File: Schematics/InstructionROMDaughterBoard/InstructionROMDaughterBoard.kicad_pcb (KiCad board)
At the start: 4 copper layers, 62.2 x 49.5 mm, 9 parts, among them J1 PC/IF Connector [0..7], J2 PC/IF Connector [8..15], J3 IROM Connector [0..7], J4 IROM Connector [8..15], U1 GLS29EE010, U2 GLS29EE010

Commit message: Instruction ROM daughter board uses same basic PCB design settings as the main board.
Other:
- net class Default: clearance 0.2 -> 0.127; trace_width 0.25 -> 0.127; via_dia 0.8 -> 0.45; via_drill 0.4 -> 0.3
- rule trace_clearance: 0.2 -> 0.127
- rule trace_min: 0.2 -> 0.0889
- rule via_min_drill: 0.3 -> 0.2
- rule via_min_size: 0.4 -> 0.45
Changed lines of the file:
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@@
   )
   (setup
-    (last_trace_width 0.25)
-    (trace_clearance 0.2)
+    (last_trace_width 0.127)
+    (trace_clearance 0.127)
     (zone_clearance 0.508)
     (zone_45_only no)
-    (trace_min 0.2)
-    (via_size 0.8)
-    (via_drill 0.4)
-    (via_min_size 0.4)
-    (via_min_drill 0.3)
+    (trace_min 0.0889)
+    (via_size 0.45)
+    (via_drill 0.3)
+    (via_min_size 0.45)
+    (via_min_drill 0.2)
     (uvia_size 0.3)
     (uvia_drill 0.1)
@@
   (net 34 /IROM8)
   (net_class Default "This is the default net class."
-    (clearance 0.2)
-    (trace_width 0.25)
-    (via_dia 0.8)
-    (via_drill 0.4)
+    (clearance 0.127)
+    (trace_width 0.127)
+    (via_dia 0.45)
+    (via_drill 0.3)
     (uvia_dia 0.3)
     (uvia_drill 0.1)
@@
     (add_net /PC_IF9)
     (add_net GND)
-    (add_net "Net-(U1-Pad1)")
-    (add_net "Net-(U1-Pad30)")
-    (add_net "Net-(U2-Pad1)")
-    (add_net "Net-(U2-Pad30)")
     (add_net VCC)
   )

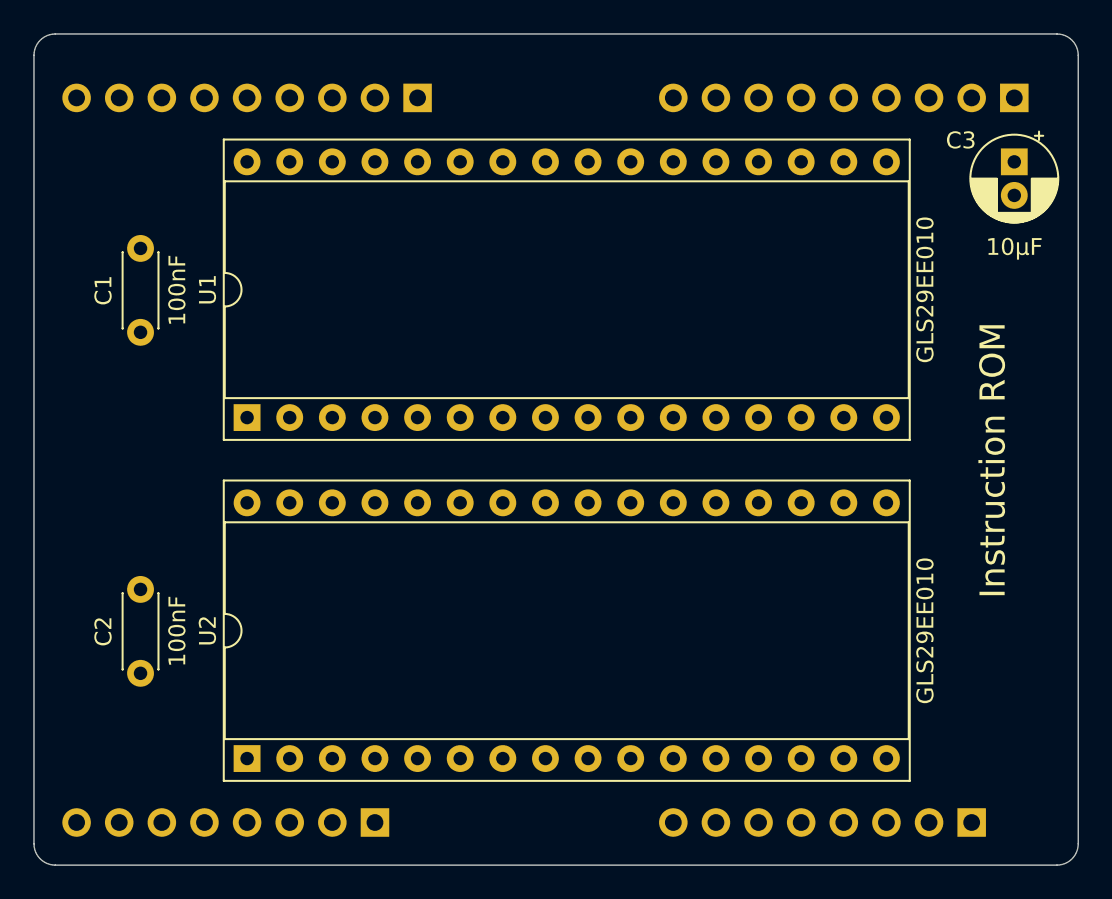
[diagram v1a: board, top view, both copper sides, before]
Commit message: checkpoint: laying out instruction rom daughter board and added power planes.
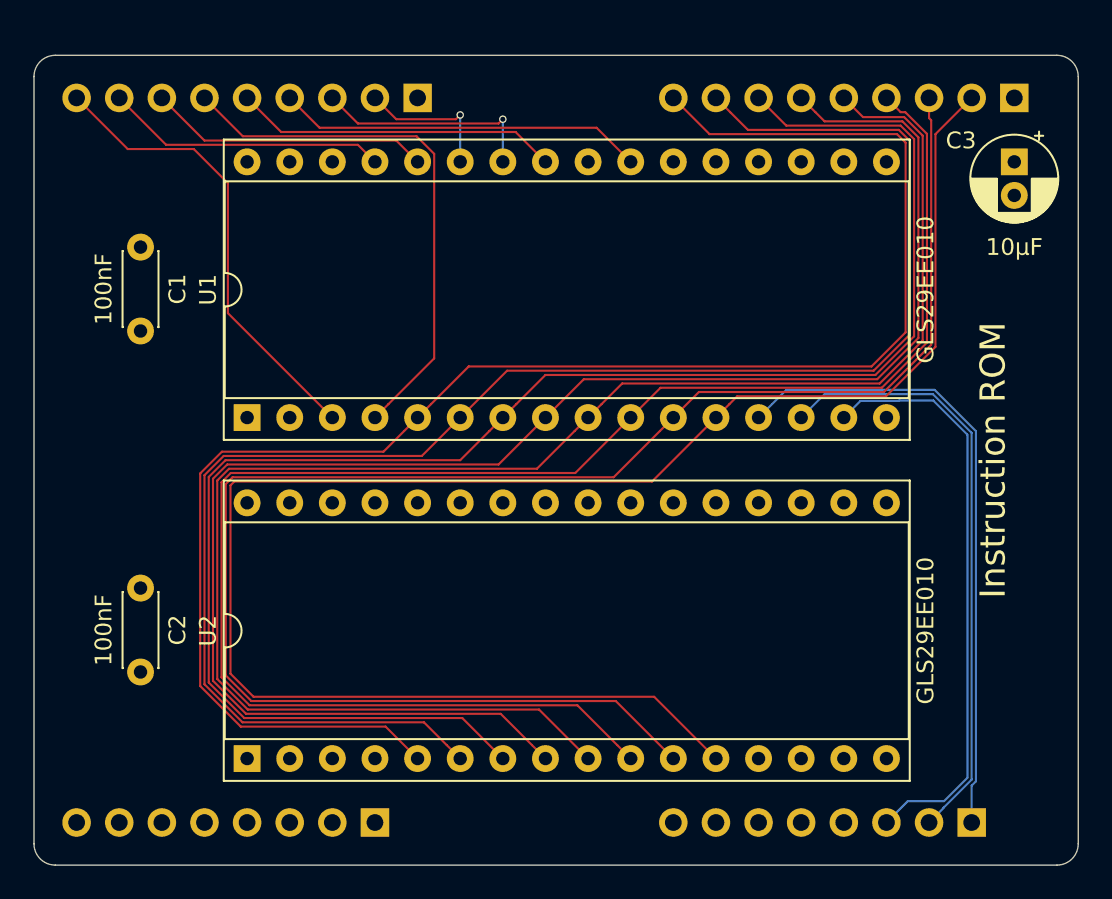
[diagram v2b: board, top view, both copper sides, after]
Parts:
- moved C1 5.08 mm to (118.1, 64.8), turned to 270 degrees
- moved C2 5.08 mm to (118.1, 85.1), turned to 270 degrees
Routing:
- net /PC_IF0: track 0.00 -> 103.4 mm
- net /PC_IF1: track 0.00 -> 100.4 mm
- net /PC_IF2: track 0.00 -> 99.2 mm
- net /PC_IF3: track 0.00 -> 99.2 mm
- net /PC_IF5: track 0.00 -> 99.2 mm
- net /PC_IF4: track 0.00 -> 99.2 mm
- net /PC_IF6: track 0.00 -> 99.2 mm
- net /PC_IF7: track 0.00 -> 99.2 mm
- net /IROM0: track 0.00 -> 38.1 mm
- net /IROM1: track 0.00 -> 36.0 mm
- net /IROM2: track 0.00 -> 35.0 mm
- net /PC_IF12: track 0.00 -> 32.2 mm
- net /PC_IF15: track 0.00 -> 27.7 mm
- net /PC_IF10: track 0.00 -> 21.9 mm
- net /PC_IF11: track 0.00 -> 19.4 mm
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- added copper zone on GND.Cu, net GND
- added copper zone on VCC.Cu, net VCC
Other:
- board size 62.2 x 49.5 mm -> 62.2 x 48.3 mm

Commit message: Finish routing Instruction ROM daughter board PCB.
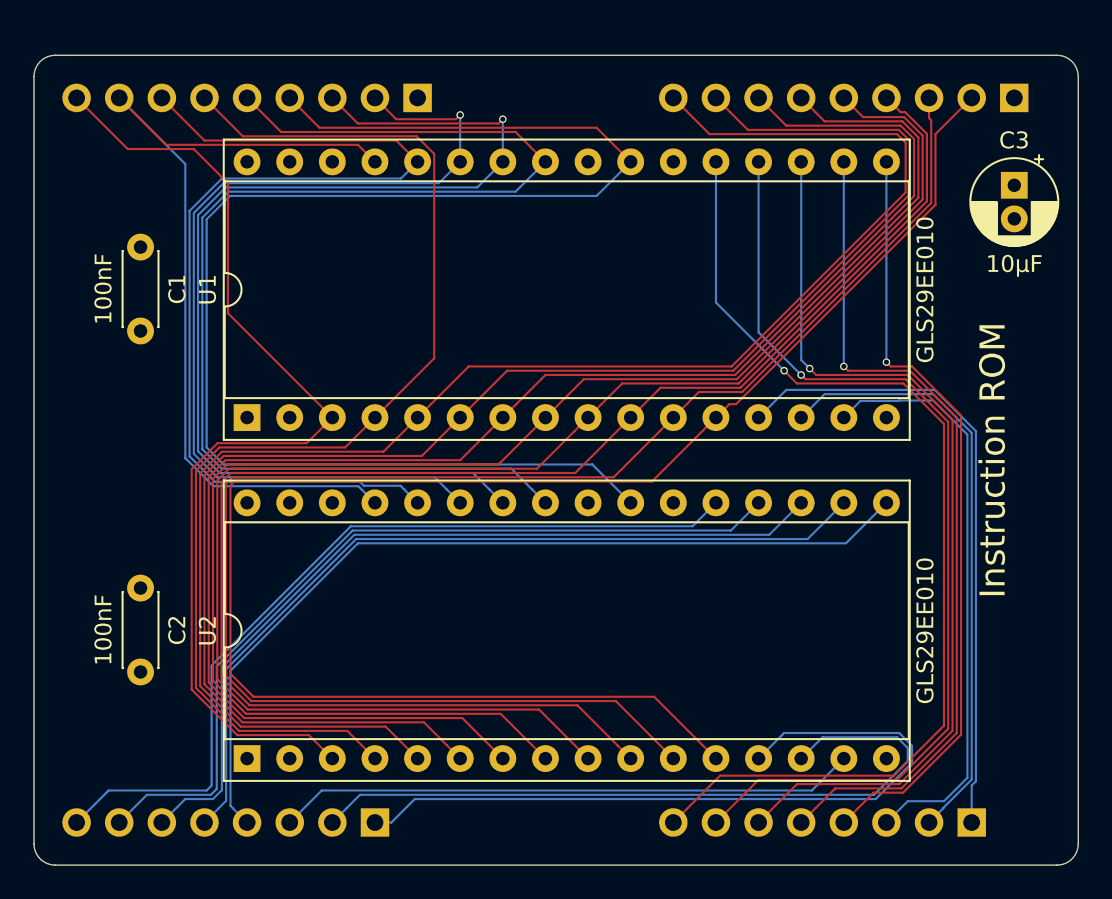
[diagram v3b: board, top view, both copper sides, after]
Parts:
- moved C3 1.40 mm to (170.2, 61.1)
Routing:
- net /PC_IF10: track 21.9 -> 88.8 mm
- net /IROM7: track 0.00 -> 61.5 mm, vias 0 -> 1
- net /IROM6: track 0.00 -> 58.1 mm, vias 0 -> 1
- net /PC_IF11: track 19.4 -> 76.8 mm
- net /IROM5: track 0.00 -> 54.7 mm, vias 0 -> 1
- net /PC_IF9: track 13.4 -> 66.4 mm
- net /IROM11: track 0.00 -> 52.7 mm
- net /IROM12: track 0.00 -> 50.6 mm
- net /IROM4: track 0.00 -> 50.5 mm, vias 0 -> 1
- net /IROM13: track 0.00 -> 50.3 mm
- net /IROM14: track 0.00 -> 50.3 mm
- net /IROM15: track 0.00 -> 50.2 mm
- net /PC_IF8: track 8.51 -> 57.1 mm
- net /IROM3: track 0.00 -> 45.9 mm, vias 0 -> 1
- net /IROM8: track 0.00 -> 44.6 mm
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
